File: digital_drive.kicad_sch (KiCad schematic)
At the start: 20 parts, among them Q1501 MMBT3904L, Q1502 MMBT3904L, Q1503 MMBT3904L, U1501 EPC23104ENGRT, U1502 EPC23104ENGRT

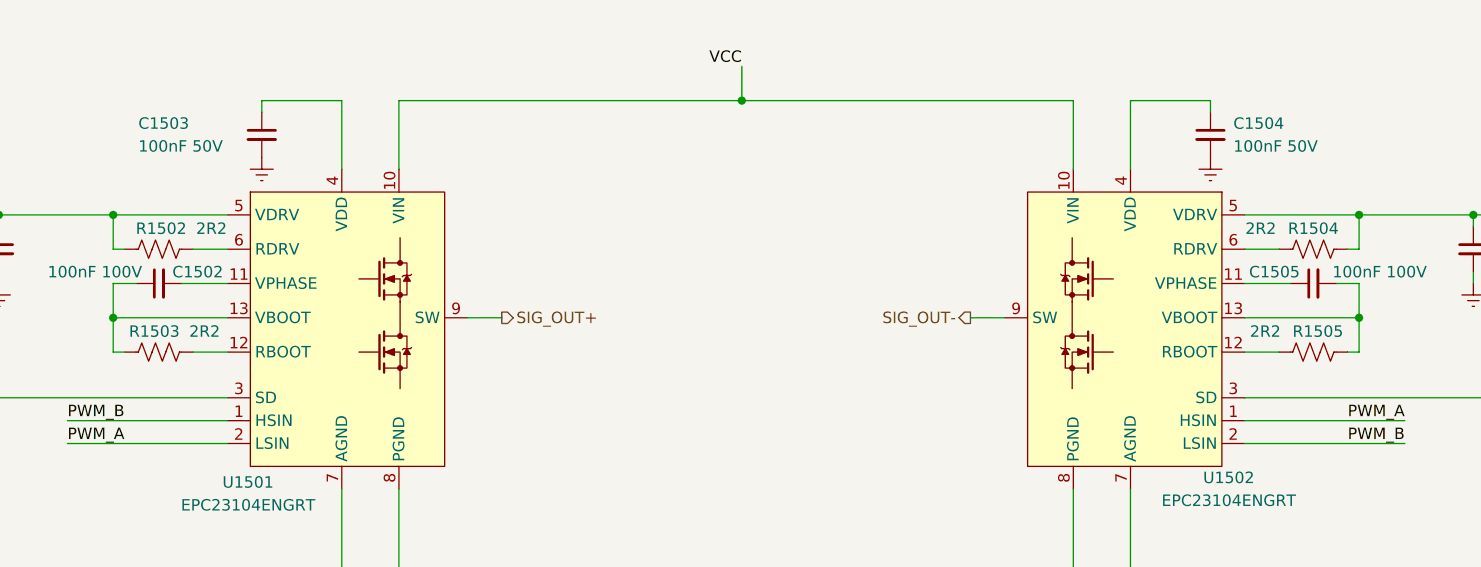
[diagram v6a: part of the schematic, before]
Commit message: Update power layout positions
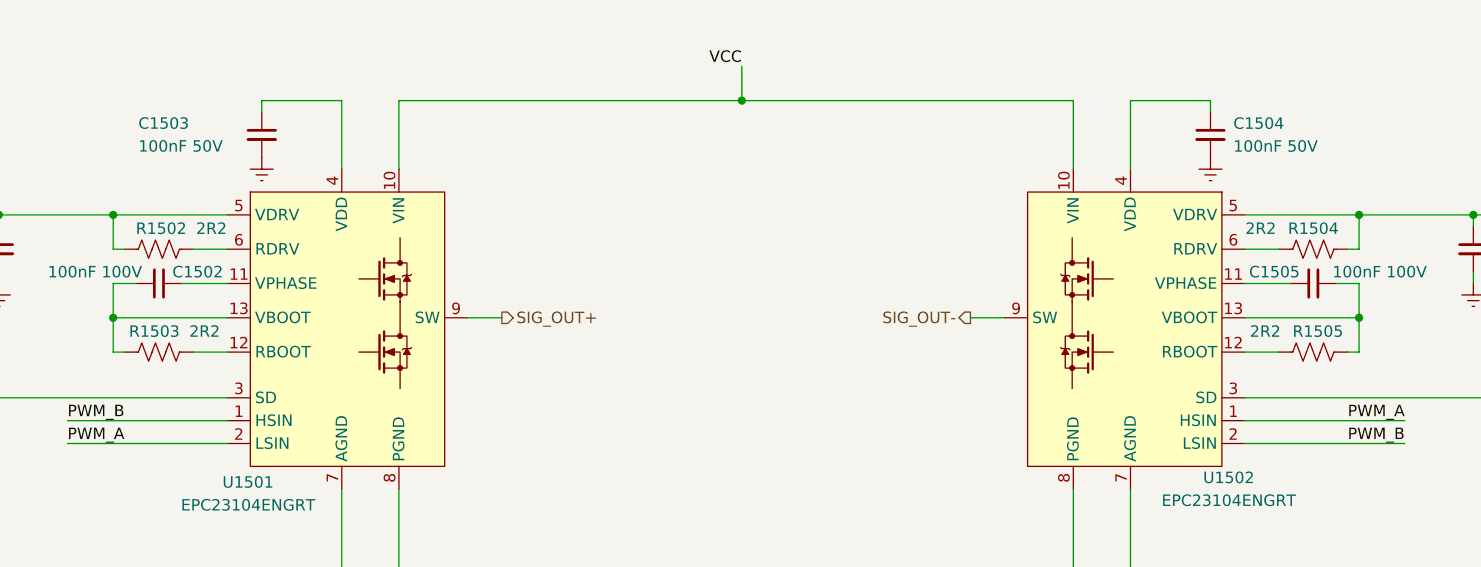
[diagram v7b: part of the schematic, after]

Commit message: Restore previous base PCB state to commit 87dd840
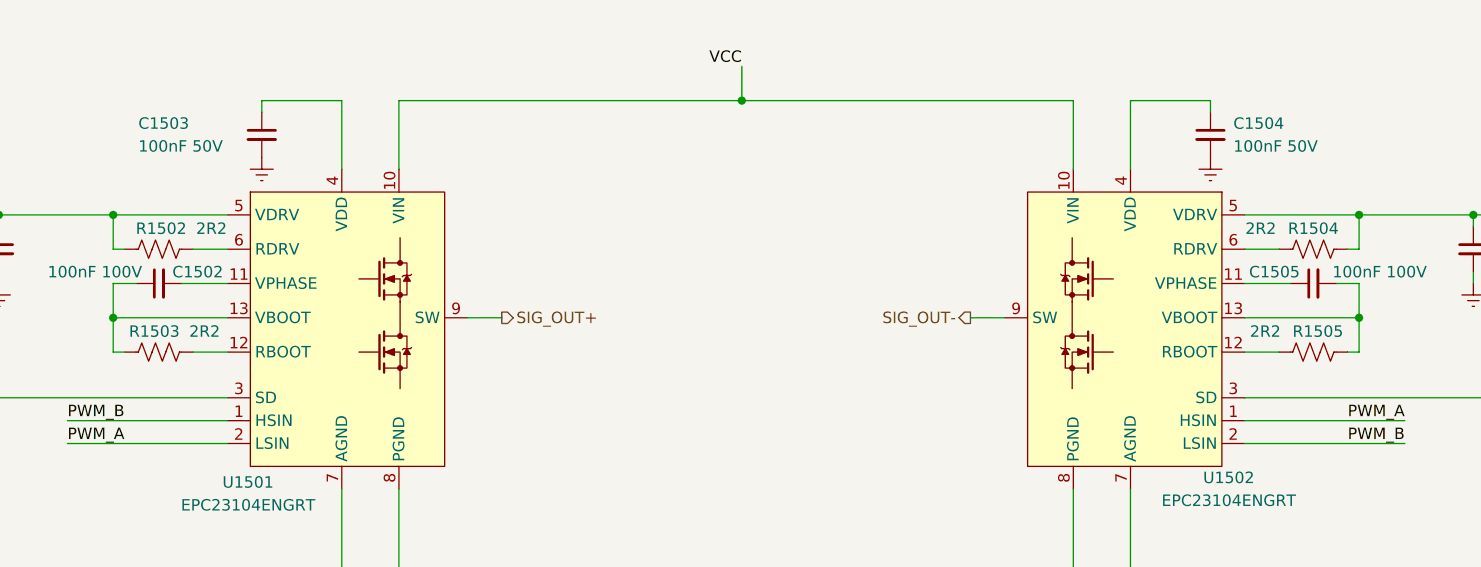
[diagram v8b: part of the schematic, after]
